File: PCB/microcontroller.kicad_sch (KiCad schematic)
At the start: 27 parts, among them IC1 STM32F479VGT6, X1 7P-26.000MBP-T

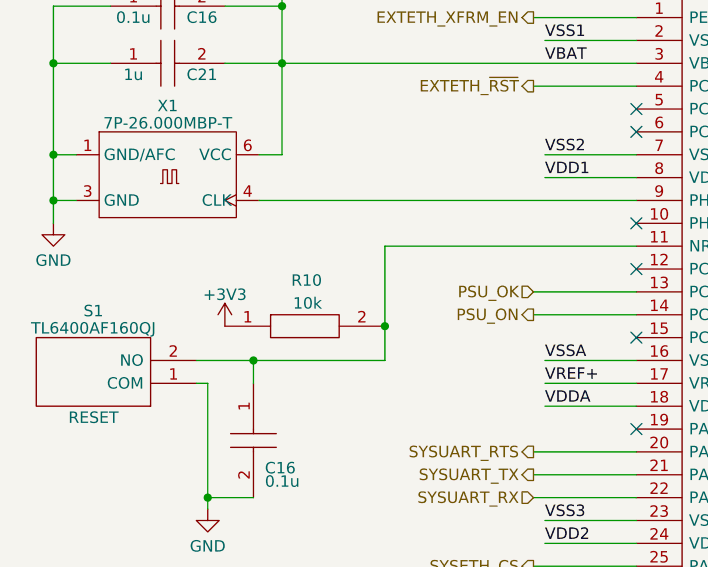
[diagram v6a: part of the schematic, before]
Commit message: switch 10k and 4.7k resistors to smaller packages (closes #32)
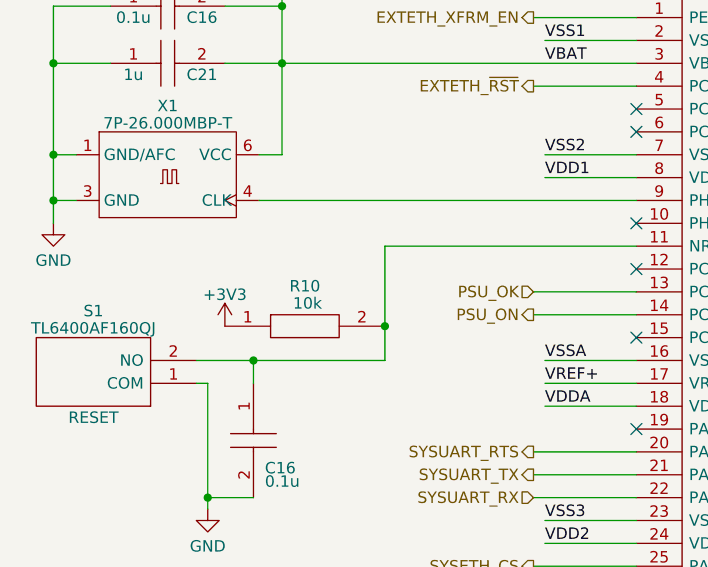
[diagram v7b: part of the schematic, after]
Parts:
- R10: footprint SamacSys_Parts:RESC5025X65N -> RESC5025X65N
- R2, R3: footprint RESC6431X65N -> RESC1005X40N; symbol SamacSys_Parts:RC2512FK-074K7L -> SamacSys_Parts:CRCW04024K70FKEDHP; Arrow Part Number RC2512FK-074K7L -> CRCW04024K70FKEDHP; Arrow Price/Stock https://www.arrow.com/en/products/rc2512fk-074k7l/yageo?reg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 -> https://www.arrow.com/en/products/crcw04024k70fkedhp/vishay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; Height 0.65 -> 0.4; Manufacturer_Name KEMET -> Vishay; Manufacturer_Part_Number RC2512FK-074K7L -> CRCW04024K70FKEDHP; Mouser Part Number 603-RC2512FK-074K7L -> 71-CRCW04024K70FKEDH; Mouser Price/Stock https://www.mouser.co.uk/ProductDetail/YAGEO/RC2512FK-074K7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 -> https://www.mouser.co.uk/ProductDetail/Vishay-Dale/CRCW0402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
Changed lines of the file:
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@@
     )
   )
-  (symbol (lib_id "SamacSys_Parts:RC2512FK-074K7L") (at 69.85 48.26 90) (unit 1)
+  (symbol (lib_id "SamacSys_Parts:CRCW04024K70FKEDHP") (at 69.85 48.26 90) (unit 1)
     (in_bom yes) (on_board yes) (dnp no)
     (property "Reference" "R3" (at 72.39 38.1 90)
@@
       (effects (font (size 1.27 1.27)) (justify right))
     )
-    (property "Footprint" "RESC6431X65N" (at 68.58 34.29 0)
-      (effects (font (size 1.27 1.27)) (justify left) hide)
-    )
-    (property "Datasheet" "https://altium.componentsearchengine.com/Datasheets/2/RC2512FK-074K7L.pdf" (at 71.12 34.29 0)
-      (effects (font (size 1.27 1.27)) (justify left) hide)
-    )
-    (property "Description" "YAGEO - RC2512FK-074K7L - SMD Chip Resistor, 2512 [6432 Metric], 4.7 kohm, RC Series, 200 V, Thick Film, 1 W" (at 73.66 34.29 0)
-      (effects (font (size 1.27 1.27)) (justify left) hide)
-    )
-    (property "Height" "0.65" (at 76.2 34.29 0)
-      (effects (font (size 1.27 1.27)) (justify left) hide)
-    )
-    (property "Manufacturer_Name" "KEMET" (at 78.74 34.29 0)
-      (effects (font (size 1.27 1.27)) (justify left) hide)
-    )
-    (property "Manufacturer_Part_Number" "RC2512FK-074K7L" (at 81.28 34.29 0)
-      (effects (font (size 1.27 1.27)) (justify left) hide)
-    )
-    (property "Mouser Part Number" "603-RC2512FK-074K7L" (at 83.82 34.29 0)
-      (effects (font (size 1.27 1.27)) (justify left) hide)
-    )
-    (property "Mouser Price/Stock" "https://www.mouser.co.uk/ProductDetail/YAGEO/RC2512FK-074K7L?qs=WeK9NnMzqvc8ESUIkdEI3A%3D%3D" (at 86.36 34.29 0)
-      (effects (font (size 1.27 1.27)) (justify left) hide)
-    )
-    (property "Arrow Part Number" "RC2512FK-074K7L" (at 88.9 34.29 0)
-      (effects (font (size 1.27 1.27)) (justify left) hide)
-    )
-    (property "Arrow Price/Stock" "https://www.arrow.com/en/products/rc2512fk-074k7l/yageo?region=nac" (at 91.44 34.29 0)
+    (property "Footprint" "RESC1005X40N" (at 68.58 34.29 0)
+      (effects (font (size 1.27 1.27)) (justify left) hide)
+    )
+    (property "Datasheet" "http://www.vishay.com/docs/20035/dcrcwe3.pdf" (at 71.12 34.29 0)
+      (effects (font (size 1.27 1.27)) (justify left) hide)
+    )
+    (property "Description" "CRCW Power Resistor 0402 0.063W 4K7 Vishay CRCW Series Thick Film Power Resistor 0402 Case 4.7k +/-1% 0.125W +/-100ppm/K" (at 73.66 34.29 0)
+      (effects (font (size 1.27 1.27)) (justify left) hide)
+    )
+    (property "Height" "0.4" (at 76.2 34.29 0)
+      (effects (font (size 1.27 1.27)) (justify left) hide)
+    )
+    (property "Manufacturer_Name" "Vishay" (at 78.74 34.29 0)
+      (effects (font (size 1.27 1.27)) (justify left) hide)
+    )
+    (property "Manufacturer_Part_Number" "CRCW04024K70FKEDHP" (at 81.28 34.29 0)
+      (effects (font (size 1.27 1.27)) (justify left) hide)
+    )
+    (property "Mouser Part Number" "71-CRCW04024K70FKEDH" (at 83.82 34.29 0)
+      (effects (font (size 1.27 1.27)) (justify left) hide)
+    )
+    (property "Mouser Price/Stock" "https://www.mouser.co.uk/ProductDetail/Vishay-Dale/CRCW04024K70FKEDHP?qs=k2%2FDWSARqgH3ASlI4vM3KQ%3D%3D" (at 86.36 34.29 0)
+      (effects (font (size 1.27 1.27)) (justify left) hide)
+    )
+    (property "Arrow Part Number" "CRCW04024K70FKEDHP" (at 88.9 34.29 0)
+      (effects (font (size 1.27 1.27)) (justify left) hide)
+    )
+    (property "Arrow Price/Stock" "https://www.arrow.com/en/products/crcw04024k70fkedhp/vishay?region=nac" (at 91.44 34.29 0)
       (effects (font (size 1.27 1.27)) (justify left) hide)
     )
@@
     )
   )
-  (symbol (lib_id "SamacSys_Parts:RC2512FK-074K7L") (at 60.96 48.26 90) (unit 1)
+  (symbol (lib_id "SamacSys_Parts:CRCW04024K70FKEDHP") (at 60.96 48.26 90) (unit 1)
     (in_bom yes) (on_board yes) (dnp no)
     (property "Reference" "R2" (at 66.04 38.1 90)
@@
       (effects (font (size 1.27 1.27)) (justify right))
     )
-    (property "Footprint" "RESC6431X65N" (at 59.69 34.29 0)
-      (effects (font (size 1.27 1.27)) (justify left) hide)
-    )
-    (property "Datasheet" "https://altium.componentsearchengine.com/Datasheets/2/RC2512FK-074K7L.pdf" (at 62.23 34.29 0)
-      (effects (font (size 1.27 1.27)) (justify left) hide)
-    )
-    (property "Description" "YAGEO - RC2512FK-074K7L - SMD Chip Resistor, 2512 [6432 Metric], 4.7 kohm, RC Series, 200 V, Thick Film, 1 W" (at 64.77 34.29 0)
-      (effects (font (size 1.27 1.27)) (justify left) hide)
-    )
-    (property "Height" "0.65" (at 67.31 34.29 0)
-      (effects (font (size 1.27 1.27)) (justify left) hide)
-    )
-    (property "Manufacturer_Name" "KEMET" (at 69.85 34.29 0)
-      (effects (font (size 1.27 1.27)) (justify left) hide)
-    )
-    (property "Manufacturer_Part_Number" "RC2512FK-074K7L" (at 72.39 34.29 0)
-      (effects (font (size 1.27 1.27)) (justify left) hide)
-    )
-    (property "Mouser Part Number" "603-RC2512FK-074K7L" (at 74.93 34.29 0)
-      (effects (font (size 1.27 1.27)) (justify left) hide)
-    )
-    (property "Mouser Price/Stock" "https://www.mouser.co.uk/ProductDetail/YAGEO/RC2512FK-074K7L?qs=WeK9NnMzqvc8ESUIkdEI3A%3D%3D" (at 77.47 34.29 0)
-      (effects (font (size 1.27 1.27)) (justify left) hide)
-    )
-    (property "Arrow Part Number" "RC2512FK-074K7L" (at 80.01 34.29 0)
-      (effects (font (size 1.27 1.27)) (justify left) hide)
-    )
-    (property "Arrow Price/Stock" "https://www.arrow.com/en/products/rc2512fk-074k7l/yageo?region=nac" (at 82.55 34.29 0)
+    (property "Footprint" "RESC1005X40N" (at 59.69 34.29 0)
+      (effects (font (size 1.27 1.27)) (justify left) hide)
+    )
+    (property "Datasheet" "http://www.vishay.com/docs/20035/dcrcwe3.pdf" (at 62.23 34.29 0)
+      (effects (font (size 1.27 1.27)) (justify left) hide)
+    )
+    (property "Description" "CRCW Power Resistor 0402 0.063W 4K7 Vishay CRCW Series Thick Film Power Resistor 0402 Case 4.7k +/-1% 0.125W +/-100ppm/K" (at 64.77 34.29 0)
+      (effects (font (size 1.27 1.27)) (justify left) hide)
+    )
+    (property "Height" "0.4" (at 67.31 34.29 0)
+      (effects (font (size 1.27 1.27)) (justify left) hide)
+    )
+    (property "Manufacturer_Name" "Vishay" (at 69.85 34.29 0)
+      (effects (font (size 1.27 1.27)) (justify left) hide)
+    )
+    (property "Manufacturer_Part_Number" "CRCW04024K70FKEDHP" (at 72.39 34.29 0)
+      (effects (font (size 1.27 1.27)) (justify left) hide)
+    )
+    (property "Mouser Part Number" "71-CRCW04024K70FKEDH" (at 74.93 34.29 0)
+      (effects (font (size 1.27 1.27)) (justify left) hide)
+    )
+    (property "Mouser Price/Stock" "https://www.mouser.co.uk/ProductDetail/Vishay-Dale/CRCW04024K70FKEDHP?qs=k2%2FDWSARqgH3ASlI4vM3KQ%3D%3D" (at 77.47 34.29 0)
+      (effects (font (size 1.27 1.27)) (justify left) hide)
+    )
+    (property "Arrow Part Number" "CRCW04024K70FKEDHP" (at 80.01 34.29 0)
+      (effects (font (size 1.27 1.27)) (justify left) hide)
+    )
+    (property "Arrow Price/Stock" "https://www.arrow.com/en/products/crcw04024k70fkedhp/vishay?region=nac" (at 82.55 34.29 0)
       (effects (font (size 1.27 1.27)) (justify left) hide)
     )
@@
       (effects (font (size 1.27 1.27)) (justify right))
     )
-    (property "Footprint" "SamacSys_Parts:RESC5025X65N" (at 102.87 184.15 0)
+    (property "Footprint" "RESC5025X65N" (at 102.87 184.15 0)
       (effects (font (size 1.27 1.27)) (justify left) hide)
     )
@@
   (symbol (lib_id "SamacSys_Parts:RC2010JK-0710KL") (at 40.64 102.87 0) (unit 1)
     (in_bom yes) (on_board yes) (dnp no)
-    (property "Reference" "R10" (at 51.435 97.79 0)
-      (effects (font (size 1.27 1.27)) (justify right))
+    (property "Reference" "R10" (at 49.53 98.425 0)
+      (effects (font (size 1.27 1.27)))
     )
     (property "Value" "10k" (at 51.435 100.33 0)
       (effects (font (size 1.27 1.27)) (justify right))
     )
-    (property "Footprint" "SamacSys_Parts:RESC5025X65N" (at 54.61 101.6 0)
+    (property "Footprint" "RESC5025X65N" (at 54.61 101.6 0)
       (effects (font (size 1.27 1.27)) (justify left) hide)
     )
@@
       (effects (font (size 1.27 1.27)) (justify right))
     )
-    (property "Footprint" "SamacSys_Parts:RESC5025X65N" (at 77.47 34.29 0)
-      (effects (font (size 1.27 1.27)) (justify left) hide)
-    )
+    (property "Footprint" "RESC5025X65N" (at 77.47 34.29 0)
+      (effects (font (size 1.27 1.27)) (justify left) hide)
+    )

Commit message: actually reduce 10k package size (ref #32)
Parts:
- R10: footprint RESC5025X65N -> RESC1005X40N; symbol SamacSys_Parts:RC2010JK-0710KL -> SamacSys_Parts:RK73H1ETTP1002F; Arrow Part Number RC2010JK-0710KL -> RK73H1ETTP1002F; Arrow Price/Stock https://www.arrow.com/en/products/rc2010jk-0710kl/yageo -> https://www.arrow.com/en/products/rk73h1ettp1002f/koa-speer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; Height 0.65 -> 0.4; Manufacturer_Name KEMET -> KOA Speer; Manufacturer_Part_Number RC2010JK-0710KL -> RK73H1ETTP1002F; Mouser Part Number 603-RC2010JK-0710KL -> 660-RK73H1ETTP1002F; Mouser Price/Stock https://www.mouser.co.uk/ProductDetail/YAGEO/RC2010JK-0710K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 -> https://www.mouser.co.uk/ProductDetail/KOA-Speer/RK73H1ETTP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
